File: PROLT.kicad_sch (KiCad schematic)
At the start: 33 parts, among them J1 64334-0100, J2 USB, M1 Module:mega-mcu100/0.3, M2 Module-vr-max9924-0.1, M3 Module-power_12and5V-0.2, U1 JDY-33

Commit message: Rev D
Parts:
- removed C28: 100n, Hellen:C0603, symbol misc:Cap
- removed U1: JDY-33, Hellen:JDY-33, symbol JDY-33:JDY-33
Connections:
- no-connect marks 48 -> 45
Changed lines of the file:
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@@
 (kicad_sch (version 20230121) (generator eeschema)
   (paper "A3")
-  (junction (at 257.81 110.49) (diameter 0) (color 0 0 0 0)
-  )
   (junction (at 130.81 177.8) (diameter 0) (color 0 0 0 0)
   )
@@
   (no_connect (at 226.06 59.69))
   (no_connect (at 157.48 69.85))
-  (no_connect (at 261.62 129.54))
   (no_connect (at 157.48 97.79))
   (no_connect (at 157.48 176.53))
   (no_connect (at 157.48 67.31))
-  (no_connect (at 261.62 135.89))
   (no_connect (at 226.06 173.99))
   (no_connect (at 129.54 182.88))
+  (no_connect (at 226.06 123.19))
   (no_connect (at 157.48 186.69))
   (no_connect (at 226.06 80.01))
+  (no_connect (at 226.06 125.73))
   (no_connect (at 226.06 151.13))
   (no_connect (at 226.06 171.45))
@@
   (no_connect (at 226.06 148.59))
   (no_connect (at 128.27 208.28))
-  (no_connect (at 261.62 139.7))
   (no_connect (at 157.48 102.87))
   (no_connect (at 157.48 133.35))
@@
   (no_connect (at 226.06 105.41))
   (no_connect (at 157.48 179.07))
-  (no_connect (at 261.62 132.08))
   (no_connect (at 157.48 72.39))
   (no_connect (at 226.06 85.09))
   (no_connect (at 157.48 209.55))
-  (no_connect (at 261.62 142.24))
   (wire (pts (xy 354.33 149.86) (xy 369.57 149.86))
     (stroke (width 0) (type default))
@@
     (stroke (width 0) (type default))
   )
-  (wire (pts (xy 289.56 110.49) (xy 278.13 110.49))
-    (stroke (width 0) (type default))
-  )
   (wire (pts (xy 265.43 156.21) (xy 266.7 156.21))
     (stroke (width 0) (type default))
@@
     (stroke (width 0) (type default))
   )
-  (wire (pts (xy 261.62 119.38) (xy 257.81 119.38))
-    (stroke (width 0) (type default))
-  )
-  (wire (pts (xy 257.81 119.38) (xy 257.81 143.51))
-    (stroke (width 0) (type default))
-  )
   (wire (pts (xy 354.33 129.54) (xy 369.57 129.54))
     (stroke (width 0) (type default))
@@
     (stroke (width 0) (type default))
   )
-  (wire (pts (xy 289.56 113.03) (xy 289.56 110.49))
-    (stroke (width 0) (type default))
-  )
   (wire (pts (xy 354.33 137.16) (xy 375.92 137.16))
     (stroke (width 0) (type default))
@@
     (stroke (width 0) (type default))
   )
-  (wire (pts (xy 226.06 125.73) (xy 261.62 125.73))
-    (stroke (width 0) (type default))
-  )
   (wire (pts (xy 157.48 217.17) (xy 157.48 219.71))
     (stroke (width 0) (type default))
@@
     (stroke (width 0) (type default))
   )
-  (wire (pts (xy 257.81 110.49) (xy 257.81 116.84))
-    (stroke (width 0) (type default))
-  )
   (wire (pts (xy 64.77 66.04) (xy 100.33 66.04))
     (stroke (width 0) (type default))
@@
     (stroke (width 0) (type default))
   )
-  (wire (pts (xy 257.81 110.49) (xy 270.51 110.49))
-    (stroke (width 0) (type default))
-  )
   (wire (pts (xy 245.11 140.97) (xy 245.11 163.83))
     (stroke (width 0) (type default))
@@
     (stroke (width 0) (type default))
   )
-  (wire (pts (xy 261.62 116.84) (xy 257.81 116.84))
-    (stroke (width 0) (type default))
-  )
   (wire (pts (xy 316.23 142.24) (xy 331.47 142.24))
     (stroke (width 0) (type default))
@@
     (stroke (width 0) (type default))
   )
-  (wire (pts (xy 257.81 107.95) (xy 257.81 110.49))
-    (stroke (width 0) (type default))
-  )
   (wire (pts (xy 64.77 59.69) (xy 100.33 59.69))
     (stroke (width 0) (type default))
@@
   )
   (wire (pts (xy 314.96 201.93) (xy 317.5 201.93))
-    (stroke (width 0) (type default))
-  )
-  (wire (pts (xy 226.06 123.19) (xy 261.62 123.19))
     (stroke (width 0) (type default))
   )
@@
         (path "/b8382448-02ab-4b6d-b574-50f724fc5555"
           (reference "TP4") (unit 1)
-        )
-      )
-    )
-  )
-  (symbol (lib_id "power:+3.3VA") (at 257.81 107.95 0) (unit 1)
-    (in_bom yes) (on_board yes) (dnp no)
-    (property "Reference" "#PWR070" (at 257.81 111.76 0)
-      (effects (font (size 1.27 1.27)) hide)
-    )
-    (property "Value" "+3.3VA" (at 257.81 104.14 0)
-      (effects (font (size 1.27 1.27)))
-    )
-    (property "Footprint" "" (at 257.81 107.95 0)
-      (effects (font (size 1.27 1.27)) hide)
-    )
-    (property "Datasheet" "" (at 257.81 107.95 0)
-      (effects (font (size 1.27 1.27)) hide)
-    )
-    (pin "1")
-    (instances
-      (project "PROLT"
-        (path "/b8382448-02ab-4b6d-b574-50f724fc5555"
-          (reference "#PWR070") (unit 1)
         )
       )
@@
     )
   )
-  (symbol (lib_id "power:GND") (at 289.56 113.03 0) (unit 1)
-    (in_bom yes) (on_board yes) (dnp no)
-    (property "Reference" "#PWR071" (at 289.56 119.38 0)
-      (effects (font (size 1.27 1.27)) hide)
-    )
-    (property "Value" "GND" (at 289.56 116.84 0)
-      (effects (font (size 1.27 1.27)))
-    )
-    (property "Footprint" "" (at 289.56 113.03 0)
-      (effects (font (size 1.27 1.27)) hide)
-    )
-    (property "Datasheet" "" (at 289.56 113.03 0)
-      (effects (font (size 1.27 1.27)) hide)
-    )
-    (pin "1")
-    (instances
-      (project "PROLT"
-        (path "/b8382448-02ab-4b6d-b574-50f724fc5555"
-          (reference "#PWR071") (unit 1)
-        )
-      )
-    )
-  )
   (symbol (lib_id "power:GNDA") (at 328.93 208.28 0) (unit 1)
     (in_bom yes) (on_board yes) (dnp no)
@@
         (path "/b8382448-02ab-4b6d-b574-50f724fc5555"
           (reference "#PWR083") (unit 1)
-        )
-      )
-    )
-  )
-  (symbol (lib_id "power:GND") (at 257.81 143.51 0) (unit 1)
-    (in_bom yes) (on_board yes) (dnp no)
-    (property "Reference" "#PWR072" (at 257.81 149.86 0)
-      (effects (font (size 1.27 1.27)) hide)
-    )
-    (property "Value" "GND" (at 257.81 147.32 0)
-      (effects (font (size 1.27 1.27)))
-    )
-    (property "Footprint" "" (at 257.81 143.51 0)
-      (effects (font (size 1.27 1.27)) hide)
-    )
-    (property "Datasheet" "" (at 257.81 143.51 0)
-      (effects (font (size 1.27 1.27)) hide)
-    )
-    (pin "1")
-    (instances
-      (project "PROLT"
-        (path "/b8382448-02ab-4b6d-b574-50f724fc5555"
-          (reference "#PWR072") (unit 1)
         )
       )
@@
     )
   )
-  (symbol (lib_id "JDY-33:JDY-33") (at 265.43 125.73 0) (unit 1)
-    (in_bom yes) (on_board yes) (dnp no) (fields_autoplaced)
-    (property "Reference" "U1" (at 284.48 127.381 0)
-      (effects (font (size 1.27 1.27)) (justify left))
-    )
-    (property "Value" "JDY-33" (at 284.48 129.921 0)
-      (effects (font (size 1.27 1.27)) (justify left))
-    )
-    (property "Footprint" "Hellen:JDY-33" (at 265.43 125.73 0)
-      (effects (font (size 1.27 1.27)) (justify left bottom) hide)
-    )
-    (property "Datasheet" "" (at 265.43 125.73 0)
-      (effects (font (size 1.27 1.27)) (justify left bottom) hide)
-    )
-    (property "PARTREV" "v1.0" (at 265.43 125.73 0)
-      (effects (font (size 1.27 1.27)) (justify left bottom) hide)
-    )
-    (property "MF" "HuiCheng" (at 265.43 125.73 0)
-      (effects (font (size 1.27 1.27)) (justify left bottom) hide)
-    )
-    (property "STANDARD" "Manufacturer Recommendations" (at 265.43 125.73 0)
-      (effects (font (size 1.27 1.27)) (justify left bottom) hide)
-    )
-    (property "LCSC" "C9900001612" (at 265.43 125.73 0)
-      (effects (font (size 1.27 1.27)) hide)
-    )
-    (pin "5")
-    (pin "2")
-    (pin "13")
-    (pin "15")
-    (pin "6")
-    (pin "17")
-    (pin "1")
-    (pin "16")
-    (pin "12")
-    (instances
-      (project "PROLT"
-        (path "/b8382448-02ab-4b6d-b574-50f724fc5555"
-          (reference "U1") (unit 1)
-        )
-      )
-    )
-  )
   (symbol (lib_id "Connector:TestPoint_Probe") (at 317.5 201.93 0) (unit 1)
     (in_bom yes) (on_board yes) (dnp no)
@@
         )
       )
-    )
-  )
-  (symbol (lib_id "misc:Cap") (at 274.32 110.49 180) (unit 1)
-    (in_bom yes) (on_board yes) (dnp no)
-    (property "Reference" "C28" (at 269.24 109.22 0)
-      (effects (font (size 1.27 1.27)) (justify right))
-    )
-    (property "Value" "100n" (at 275.59 109.22 0)
-      (effects (font (size 1.27 1.27)) (justify right))
-    )
-    (property "Footprint" "Hellen:C0603" (at 276.86 106.68 0)
-      (effects (font (size 1.27 1.27)) hide)
-    )
-    (property "Datasheet" "" (at 278.13 110.49 90)
-      (effects (font (size 1.27 1.27)) hide)
-    )
-    (property "LCSC" "C14663" (at 274.32 110.49 0)
-      (effects (font (size 1.27 1.27)) hide)
-    )
-    (pin "1")
-    (pin "2")
-    (instances
-      (project "PROLT"
-        (path "/b8382448-02ab-4b6d-b574-50f724fc5555"
-          (reference "C28") (unit 1)
-        )
-      )

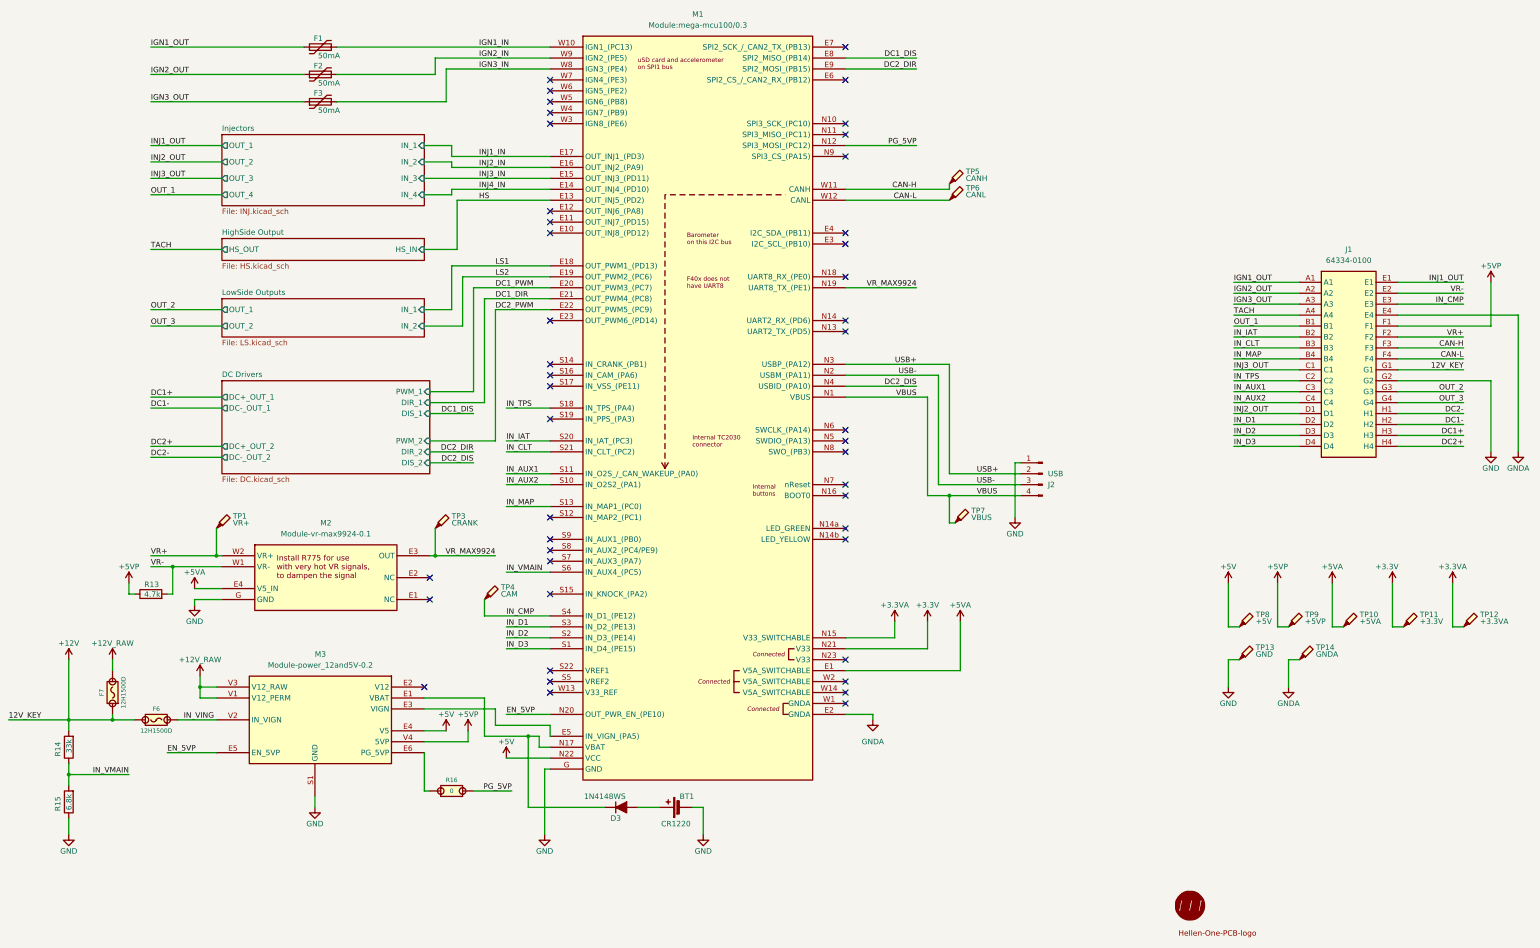
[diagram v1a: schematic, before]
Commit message: Rev E
Back to VNLD5160TR-E, 1 channel per injector now
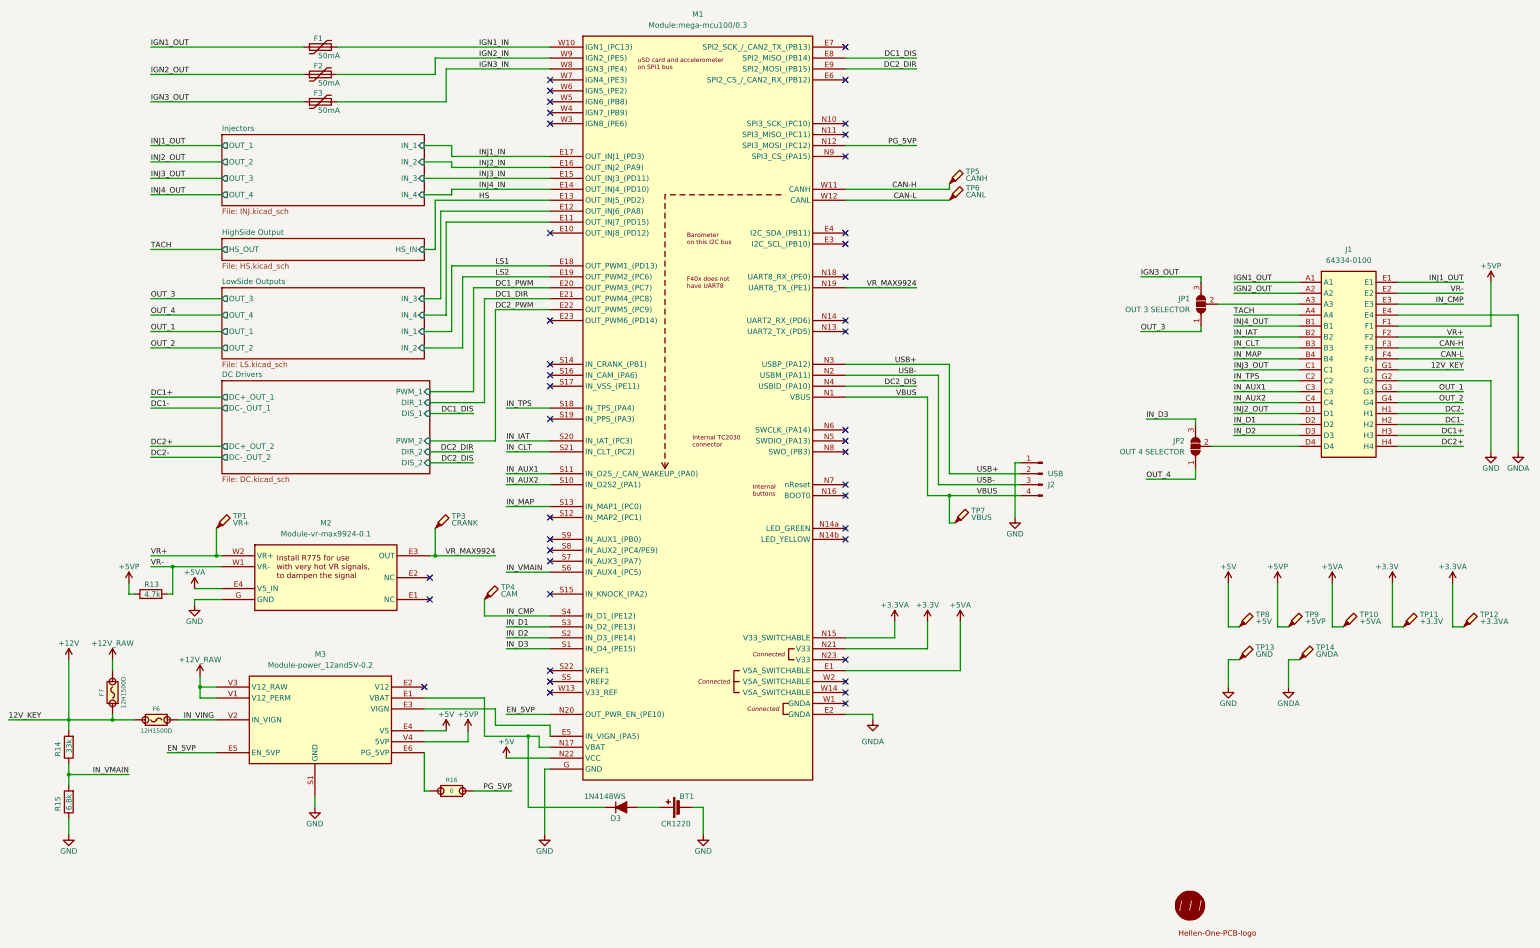
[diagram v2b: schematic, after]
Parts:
- added JP1: OUT 3 SELECTOR, Jumper:SolderJumper-3_P2.0mm_Open_TrianglePad1.0x1.5mm, symbol Jumper:SolderJumper_3_Open
- added JP2: OUT 4 SELECTOR, Jumper:SolderJumper-3_P2.0mm_Open_TrianglePad1.0x1.5mm, symbol Jumper:SolderJumper_3_Open
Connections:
- net IGN3_OUT: now also JP1.3 (B); no longer J1.A3
- net IN_D3: now also JP2.3 (B); no longer J1.D4
- net OUT_1: now also J1.G3; no longer J1.B1
- net OUT_2: now also J1.G4; no longer J1.G3
- net OUT_3: now also JP1.1 (A); no longer J1.G4
- net LowSide Outputs/IN_4: now reaches M1.E11 (OUT_INJ7_(PD15))
- net LowSide Outputs/IN_3: now reaches M1.E12 (OUT_INJ6_(PA8))
- new net: J1.A3, JP1.2 (C)
- new net: J1.D4, JP2.2 (C)
- new net INJ4_OUT: J1.B1
- new net OUT_4: JP2.1 (A)
- no-connect marks 45 -> 43
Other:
- sheet LowSide Outputs ports: added IN_3, IN_4, OUT_3, OUT_4; removed none
